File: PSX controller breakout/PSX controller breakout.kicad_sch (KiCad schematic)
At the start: 6 parts, among them J2 Conn_01x10_MountingPin, J3 Conn_01x04_MountingPin, J4 Conn_01x10_Pin

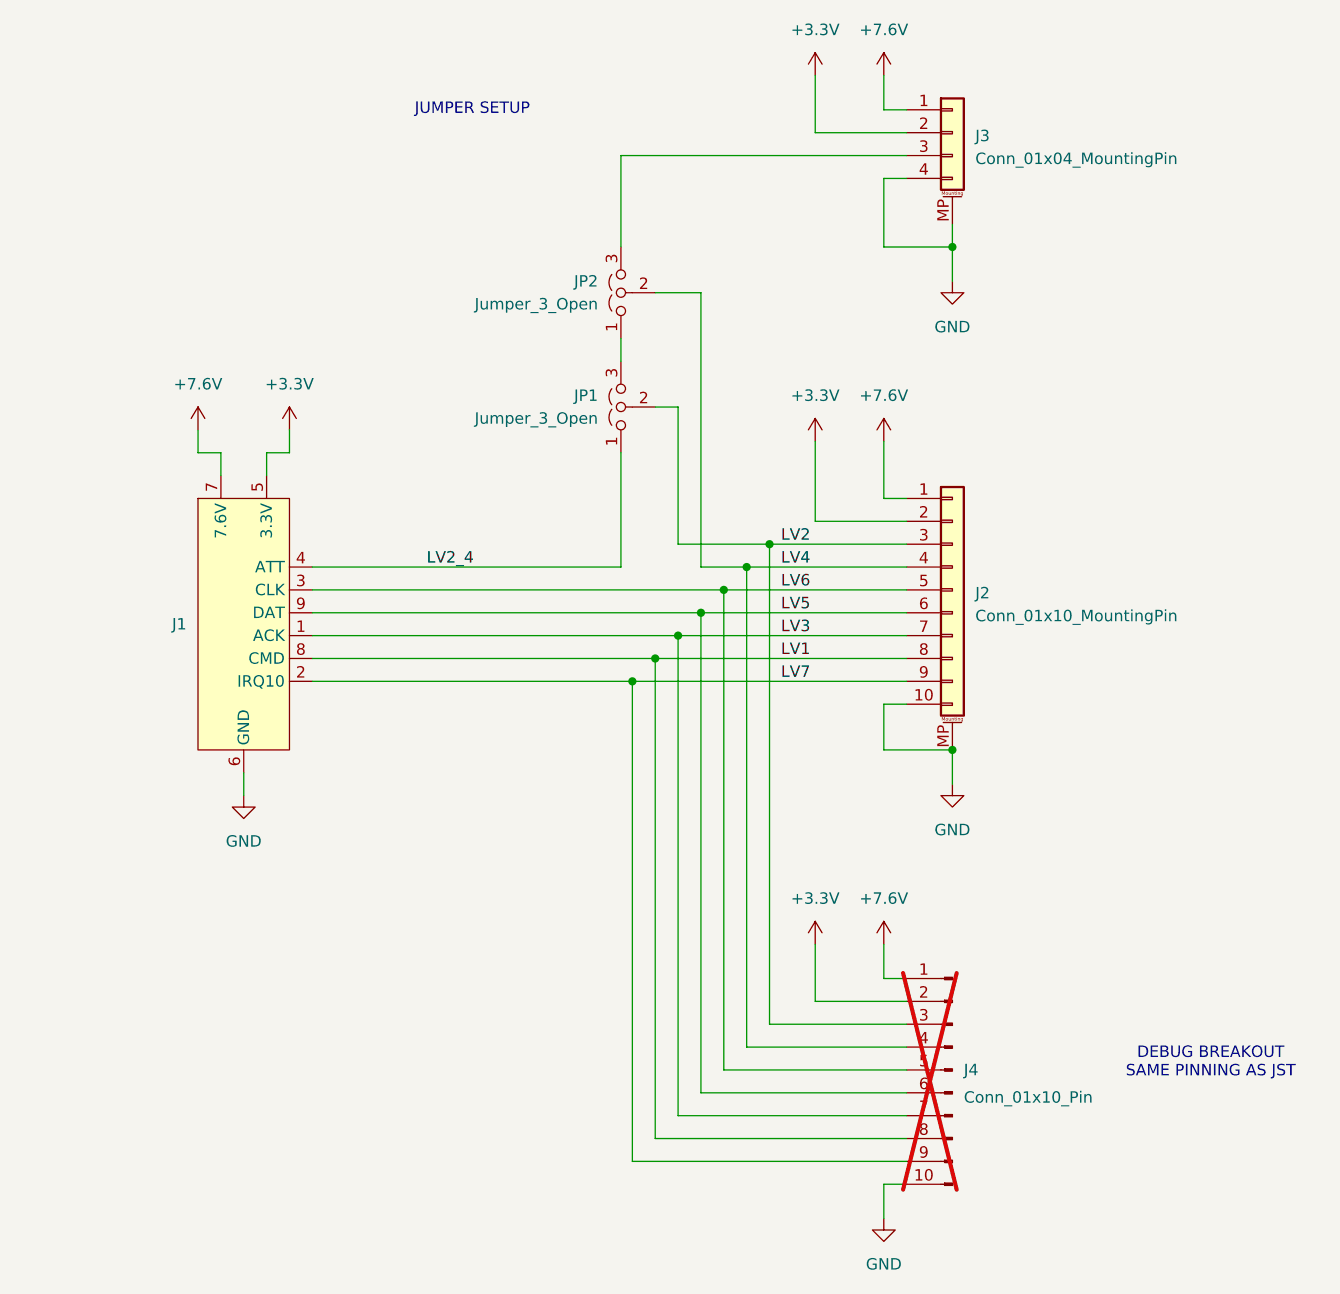
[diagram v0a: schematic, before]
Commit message: renamed PS1 files to PSX
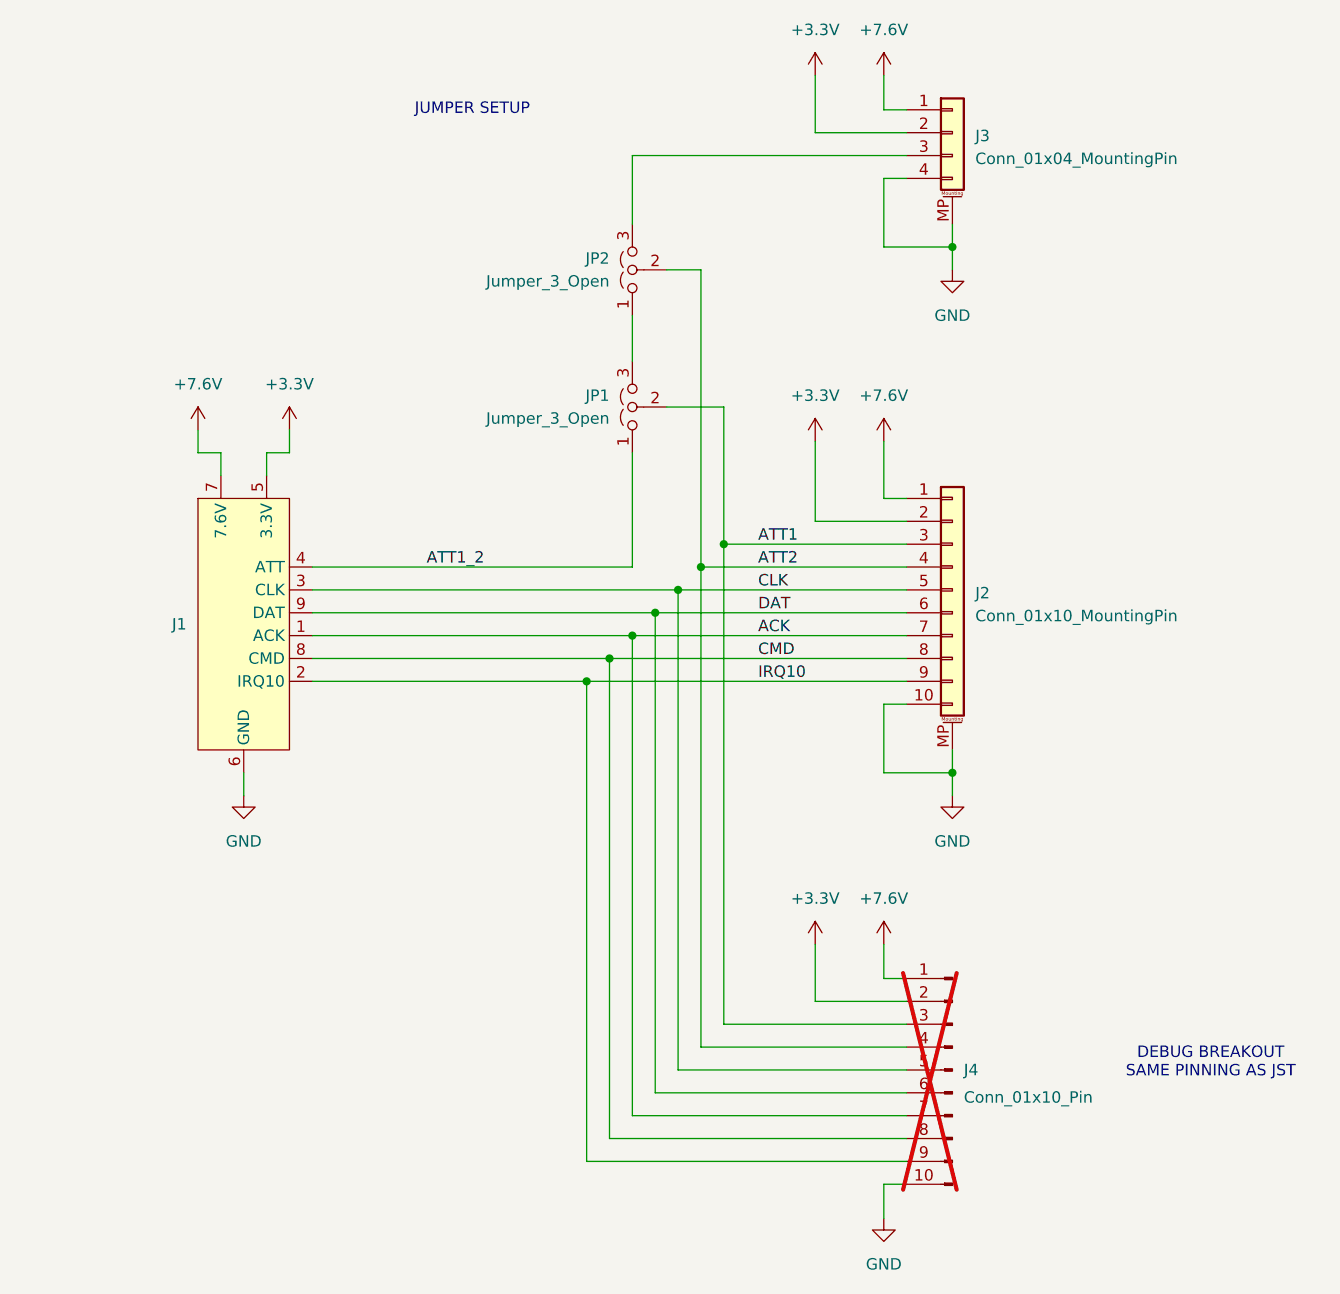
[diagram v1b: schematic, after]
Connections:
- net LV1 renamed CMD
- net LV2 renamed ATT1
- net LV2_4 renamed ATT1_2
- net LV3 renamed ACK
- net LV4 renamed ATT2
- net LV5 renamed DAT
- net LV6 renamed CLK
- net LV7 renamed IRQ10
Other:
- moved on the sheet: JP1, JP2

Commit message: assigned footprints
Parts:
- J4: footprint (none) -> Connector_PinSocket_2.54mm:PinSocket_1x10_P2.54mm_Vertical
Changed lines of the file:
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@@
 			)
 		)
-		(property "Footprint" ""
+		(property "Footprint" "Connector_PinSocket_2.54mm:PinSocket_1x10_P2.54mm_Vertical"
 			(at 220.98 175.26 0)
 			(hide yes)

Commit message: assigned footprints
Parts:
- J2: footprint (none) -> Connector_JST:JST_PH_S10B-PH-SM4-TB_1x10-1MP_P2.00mm_Horizontal
- J3: footprint (none) -> Connector_JST:JST_PH_S4B-PH-SM4-TB_1x04-1MP_P2.00mm_Horizontal
- JP1, JP2: footprint (none) -> Jumper:SolderJumper-3_P1.3mm_Open_Pad1.0x1.5mm_NumberLabels
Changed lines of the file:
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@@
 			)
 		)
-		(property "Footprint" ""
+		(property "Footprint" "Connector_JST:JST_PH_S4B-PH-SM4-TB_1x04-1MP_P2.00mm_Horizontal"
 			(at 220.98 71.12 0)
 			(hide yes)
@@
 			)
 		)
-		(property "Footprint" ""
+		(property "Footprint" "Connector_JST:JST_PH_S10B-PH-SM4-TB_1x10-1MP_P2.00mm_Horizontal"
 			(at 220.98 121.92 0)
 			(hide yes)
@@
 			)
 		)
-		(property "Footprint" ""
+		(property "Footprint" "Jumper:SolderJumper-3_P1.3mm_Open_Pad1.0x1.5mm_NumberLabels"
 			(at 185.42 101.6 0)
 			(hide yes)
@@
 			)
 		)
-		(property "Footprint" ""
+		(property "Footprint" "Jumper:SolderJumper-3_P1.3mm_Open_Pad1.0x1.5mm_NumberLabels"
 			(at 185.42 86.36 0)
 			(hide yes)

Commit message: Assigned PSX footprint and started layout
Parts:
- J1: value (none) -> PSX Connector 1P; footprint (none) -> Penny_Connectors:PSX Connector 1P
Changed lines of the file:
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@@
 		(in_pos_files yes)
 		(dnp no)
-		(fields_autoplaced yes)
 		(property "Reference" "J1"
 			(at 135.89 125.7299 0)
@@
 			)
 		)
-		(property "Value" ""
-			(at 137.16 111.76 0)
+		(property "Value" "PSX Connector 1P"
+			(at 127.254 128.27 0)
 			(show_name no)
 			(do_not_autoplace no)
@@
 			)
 		)
-		(property "Footprint" ""
+		(property "Footprint" "Penny_Connectors:PSX Connector 1P"
 			(at 137.16 111.76 0)
 			(hide yes)
